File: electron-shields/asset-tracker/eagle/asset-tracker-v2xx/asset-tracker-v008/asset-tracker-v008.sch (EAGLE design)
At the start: 47 parts, among them J1 1X2-3.5MM, Q1 MPSA42, T1 DMG3415, U1 MAX-M8, U3 LIS3DHTR, U4 RF_SWITCHSC-70-6, U5 SAFFB1G56KB0F0A, U6 BGA725L6-ALT, X1 ELECTRON, X2 IPEX-20279-001E

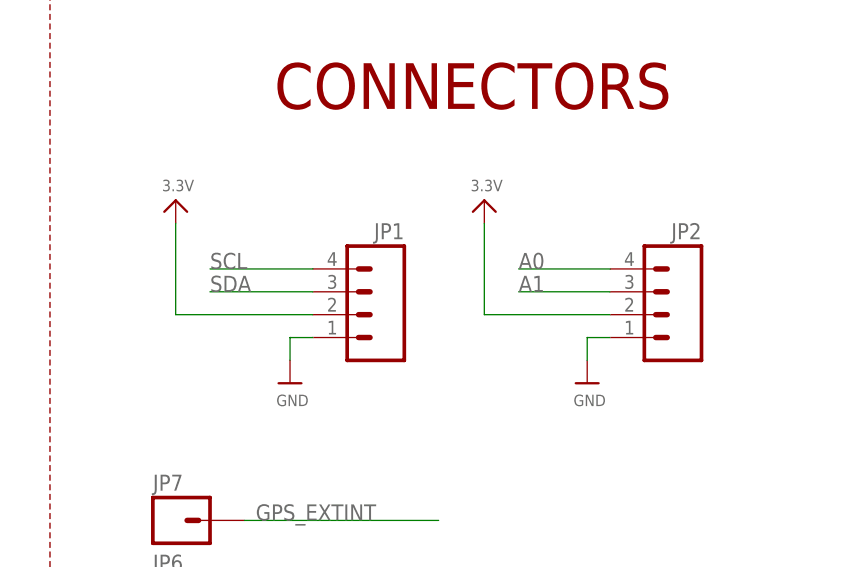
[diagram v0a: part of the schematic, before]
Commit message: update the grove connector again,make the latch face the edge of the board
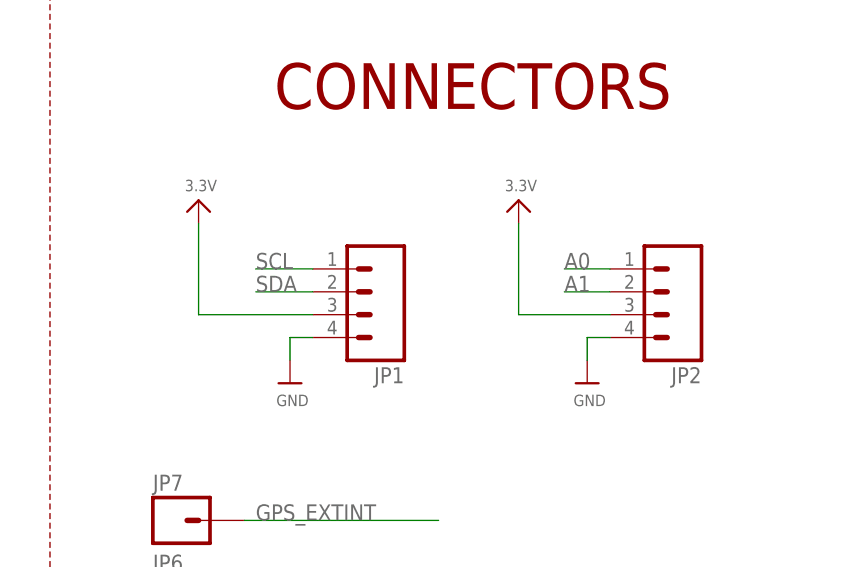
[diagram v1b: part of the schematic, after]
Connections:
- net 3.3V: now also JP1.3, JP2.3; no longer JP1.2, JP2.2
- net A0: now also JP2.1; no longer JP2.4
- net A1: now also JP2.2; no longer JP2.3
- net GND: now also JP1.4, JP2.4; no longer JP1.1, JP2.1
- net SCL: now also JP1.1; no longer JP1.4
- net SDA: now also JP1.2; no longer JP1.3
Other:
- moved on the sheet: JP1, JP2
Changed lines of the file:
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@@
 <instance part="U$20" gate="G$1" x="354.33" y="179.07"/>
 <instance part="U$22" gate="G$1" x="314.96" y="85.09"/>
-<instance part="U$23" gate="G$1" x="302.26" y="105.41"/>
+<instance part="U$23" gate="G$1" x="304.8" y="105.41"/>
 <instance part="U$24" gate="G$1" x="347.98" y="85.09"/>
-<instance part="U$25" gate="G$1" x="336.55" y="105.41"/>
+<instance part="U$25" gate="G$1" x="340.36" y="105.41"/>
 <instance part="A1" gate="ANT" x="48.26" y="193.04"/>
 <instance part="U$26" gate="G$1" x="354.33" y="189.23" rot="R90"/>
 <instance part="R3" gate="G$1" x="302.26" y="218.44" rot="R90"/>
-<instance part="JP2" gate="G$1" x="355.6" y="92.71" rot="MR0"/>
-<instance part="JP1" gate="G$1" x="322.58" y="92.71" rot="MR0"/>
+<instance part="JP2" gate="G$1" x="355.6" y="95.25" rot="R180"/>
+<instance part="JP1" gate="G$1" x="322.58" y="95.25" rot="R180"/>
 <instance part="U$27" gate="G$1" x="121.92" y="161.29"/>
 <instance part="U$28" gate="G$1" x="43.18" y="185.42"/>
@@
 </segment>
 <segment>
-<wire x1="317.5" y1="90.17" x2="314.96" y2="90.17" width="0.1524" layer="91"/>
 <wire x1="314.96" y1="90.17" x2="314.96" y2="87.63" width="0.1524" layer="91"/>
 <pinref part="U$22" gate="G$1" pin="GND"/>
-<pinref part="JP1" gate="G$1" pin="1"/>
-</segment>
-<segment>
-<wire x1="350.52" y1="90.17" x2="347.98" y2="90.17" width="0.1524" layer="91"/>
+<pinref part="JP1" gate="G$1" pin="4"/>
+<wire x1="317.5" y1="90.17" x2="314.96" y2="90.17" width="0.1524" layer="91"/>
+</segment>
+<segment>
 <wire x1="347.98" y1="90.17" x2="347.98" y2="87.63" width="0.1524" layer="91"/>
 <pinref part="U$24" gate="G$1" pin="GND"/>
-<pinref part="JP2" gate="G$1" pin="1"/>
+<pinref part="JP2" gate="G$1" pin="4"/>
+<wire x1="350.52" y1="90.17" x2="347.98" y2="90.17" width="0.1524" layer="91"/>
 </segment>
 <segment>
@@
 </segment>
 <segment>
-<wire x1="302.26" y1="92.71" x2="302.26" y2="102.87" width="0.1524" layer="91"/>
+<wire x1="304.8" y1="92.71" x2="304.8" y2="102.87" width="0.1524" layer="91"/>
 <pinref part="U$23" gate="G$1" pin="3.3V"/>
-<pinref part="JP1" gate="G$1" pin="2"/>
-<wire x1="317.5" y1="92.71" x2="302.26" y2="92.71" width="0.1524" layer="91"/>
-</segment>
-<segment>
-<wire x1="350.52" y1="92.71" x2="336.55" y2="92.71" width="0.1524" layer="91"/>
-<wire x1="336.55" y1="92.71" x2="336.55" y2="102.87" width="0.1524" layer="91"/>
+<pinref part="JP1" gate="G$1" pin="3"/>
+<wire x1="317.5" y1="92.71" x2="304.8" y2="92.71" width="0.1524" layer="91"/>
+</segment>
+<segment>
+<wire x1="340.36" y1="92.71" x2="340.36" y2="102.87" width="0.1524" layer="91"/>
 <pinref part="U$25" gate="G$1" pin="3.3V"/>
-<pinref part="JP2" gate="G$1" pin="2"/>
+<pinref part="JP2" gate="G$1" pin="3"/>
+<wire x1="350.52" y1="92.71" x2="340.36" y2="92.71" width="0.1524" layer="91"/>
 </segment>
 <segment>
@@
 <net name="SCL" class="0">
 <segment>
-<wire x1="317.5" y1="97.79" x2="306.07" y2="97.79" width="0.1524" layer="91"/>
-<label x="306.07" y="97.79" size="1.778" layer="95"/>
-<pinref part="JP1" gate="G$1" pin="4"/>
-</segment>
-<segment>
 <pinref part="X1" gate="G$1" pin="D1"/>
 <wire x1="223.52" y1="58.42" x2="237.49" y2="58.42" width="0.1524" layer="91"/>
 <label x="228.6" y="58.42" size="1.778" layer="95"/>
 </segment>
+<segment>
+<pinref part="JP1" gate="G$1" pin="1"/>
+<wire x1="317.5" y1="97.79" x2="311.15" y2="97.79" width="0.1524" layer="91"/>
+<label x="311.15" y="97.79" size="1.778" layer="95"/>
+</segment>
 </net>
 <net name="SDA" class="0">
-<segment>
-<wire x1="317.5" y1="95.25" x2="306.07" y2="95.25" width="0.1524" layer="91"/>
-<label x="306.07" y="95.25" size="1.778" layer="95"/>
-<pinref part="JP1" gate="G$1" pin="3"/>
-</segment>
 <segment>
 <pinref part="X1" gate="G$1" pin="D0"/>
@@
 <label x="228.6" y="55.88" size="1.778" layer="95"/>
 </segment>
+<segment>
+<pinref part="JP1" gate="G$1" pin="2"/>
+<wire x1="317.5" y1="95.25" x2="311.15" y2="95.25" width="0.1524" layer="91"/>
+<label x="311.15" y="95.25" size="1.778" layer="95"/>
+</segment>
 </net>
 <net name="A0" class="0">
@@
 </segment>
 <segment>
-<wire x1="350.52" y1="97.79" x2="340.36" y2="97.79" width="0.1524" layer="91"/>
-<label x="340.36" y="97.79" size="1.778" layer="95"/>
-<pinref part="JP2" gate="G$1" pin="4"/>
+<pinref part="JP2" gate="G$1" pin="1"/>
+<wire x1="350.52" y1="97.79" x2="345.44" y2="97.79" width="0.1524" layer="91"/>
+<label x="345.44" y="97.79" size="1.778" layer="95"/>
 </segment>
 </net>
@@
 </segment>
 <segment>
-<wire x1="350.52" y1="95.25" x2="340.36" y2="95.25" width="0.1524" layer="91"/>
-<label x="340.36" y="95.25" size="1.778" layer="95"/>
-<pinref part="JP2" gate="G$1" pin="3"/>
-</segment>
-</net>
+<pinref part="JP2" gate="G$1" pin="2"/>
+<wire x1="350.52" y1="95.25" x2="345.44" y2="95.25" width="0.1524" layer="91"/>
+<label x="345.44" y="95.25" size="1.778" layer="95"/>
+</segment>
+</net>
